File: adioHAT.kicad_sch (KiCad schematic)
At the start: 25 parts, among them J2 Conn_02x02_Odd_Even, J3 Conn_02x20_Odd_Even, J4 Conn_01x01, J4 Conn_02x20_Odd_Even, U2 AD5693RxRM, U2 PCA9575D, U3 AD5593R, U4 LM7321, U5 AD8603, U6 TXU0104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

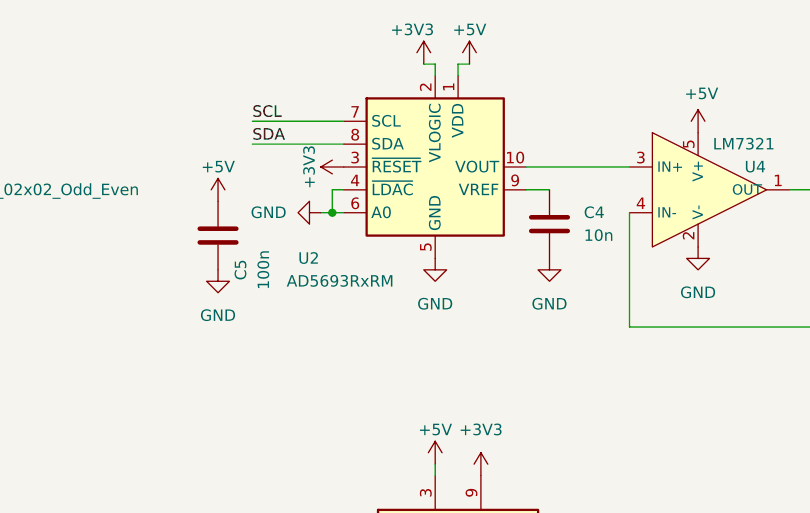
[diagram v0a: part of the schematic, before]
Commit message: exchanged DAC IC
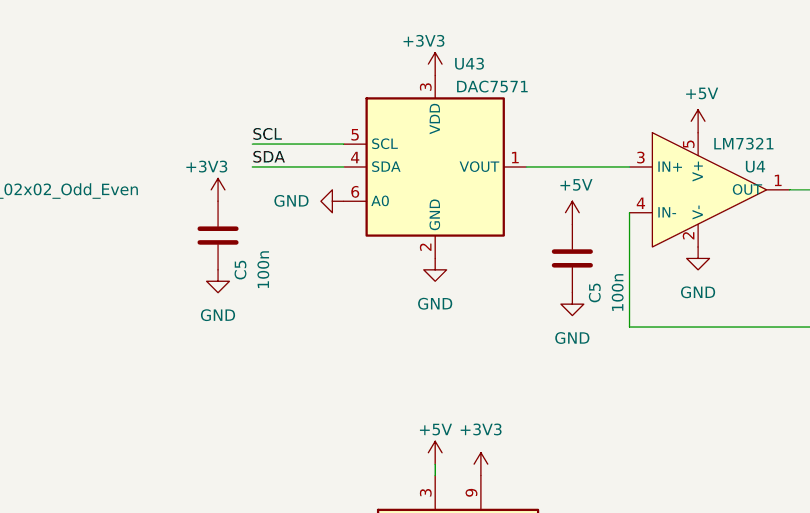
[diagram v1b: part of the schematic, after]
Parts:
- removed C4: 10n, Capacitor_SMD:C_0603_1608Metric, symbol Device:C
- removed U2: AD5693RxRM, Package_SO:MSOP-10_3x3mm_P0.5mm, symbol Analog_DAC:AD5693RxRM
- added C5: 100n, Capacitor_SMD:C_0603_1608Metric, symbol Device:C
- added U43: DAC7571, Package_TO_SOT_SMD:SOT-23-6, symbol yku_symbols:DAC7571
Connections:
- net +3V3: now also C5.2, U43.3 (VDD)
- net +5V: now also C5.2; no longer C5.2
- net GND: now also C5.1, U43.2 (GND), U43.6 (A0)
- net SCL: now also U43.5 (SCL)
- net SDA: now also U43.4 (SDA)
- net at U4.3 (IN+): now also U43.1 (VOUT)

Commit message: fixed i2c connections for ad5593
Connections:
- net SCL: now also U3.16 (SCL); no longer U3.15 (SDA)
- net SDA: now also U3.15 (SDA); no longer U3.16 (SCL)
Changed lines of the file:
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@@
     (effects (font (size 1.27 1.27)) (justify left bottom))
   )
-  (label "SDA" (at 66.04 76.2 0) (fields_autoplaced)
+  (label "SCL" (at 66.04 76.2 0) (fields_autoplaced)
     (effects (font (size 1.27 1.27)) (justify left bottom))
   )
@@
     (effects (font (size 1.27 1.27)) (justify left bottom))
   )
-  (label "SCL" (at 66.04 73.66 0) (fields_autoplaced)
+  (label "SDA" (at 66.04 73.66 0) (fields_autoplaced)
     (effects (font (size 1.27 1.27)) (justify left bottom))
   )
